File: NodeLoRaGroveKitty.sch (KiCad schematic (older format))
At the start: 37 parts, among them P1 PICKIT PROGRAMMER, P2 Battery, P3 A0, P4 D9, P5 USB-Serial, P6 I2C, SW1 SW_PUSH, SW2 SW_PUSH, U1 AP2112, U2 MCP73831T-2ATI/OT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

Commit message: Fix ADC pin
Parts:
- MODULE1: footprint Library:RN2483 -> TIH:RN2483
- SW1: value SW_PUSH -> SW_BOOT; footprint TIH:SW_SPST_KMR2 -> TIH:SW_B3U-1000P
- SW2: value SW_PUSH -> SW_RESET; footprint TIH:SW_SPST_KMR2 -> TIH:SW_B3U-1000P
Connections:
- net A0: no longer P3.4 (P4)
- net ADC: now also P3.4 (P4)
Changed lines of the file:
@@
 F 0 "MODULE1" H 1650 3550 50  0000 L CNN
 F 1 "RN2903" H 1650 750 50  0000 L CNN
-F 2 "Library:RN2483" H 2250 2150 50  0001 L CNN
+F 2 "TIH:RN2483" H 2250 2150 50  0001 L CNN
 F 3 "None" H 2250 2150 50  0001 L CNN
 F 4 "Sub-GHz Dual Band Long Range Transceiver LoRa Module" H 2250 2150 50  0001 L CNN "Description"
@@
 P 4850 1400
 F 0 "SW2" H 5000 1510 50  0000 C CNN
-F 1 "SW_PUSH" H 4850 1320 50  0000 C CNN
-F 2 "TIH:SW_SPST_KMR2" H 4850 1400 50  0001 C CNN
+F 1 "SW_RESET" H 4850 1320 50  0000 C CNN
+F 2 "TIH:SW_B3U-1000P" H 4850 1400 50  0001 C CNN
 F 3 "" H 4850 1400 50  0000 C CNN
 	1    4850 1400
@@
 $EndComp
 Text Label 9300 5400 0    60   ~ 0
-A0
+ADC
 $Comp
 L GND #PWR017
@@
 P 4830 1965
 F 0 "SW1" H 4980 2075 50  0000 C CNN
-F 1 "SW_PUSH" H 4830 1885 50  0000 C CNN
-F 2 "TIH:SW_SPST_KMR2" H 4830 1965 50  0001 C CNN
+F 1 "SW_BOOT" H 4830 1885 50  0000 C CNN
+F 2 "TIH:SW_B3U-1000P" H 4830 1965 50  0001 C CNN
 F 3 "" H 4830 1965 50  0000 C CNN
 	1    4830 1965

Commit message: Update Grove to 5v
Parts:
- D5: footprint Diodes_SMD:SMA_Handsoldering -> Diodes_SMD:SMB_Handsoldering
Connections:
- net +3V3: no longer P3.2 (P2), P4.2 (P2), P6.2 (P2)
- net A0: now also P3.4 (P4)
- net ADC: no longer P3.4 (P4)
- net VCC: now also P3.2 (P2), P4.2 (P2), P6.2 (P2)
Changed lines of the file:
@@
 $EndComp
 Text Label 9300 5400 0    60   ~ 0
-ADC
+A0
 $Comp
 L GND #PWR017
@@
 $EndComp
 $Comp
-L +3.3V #PWR030
-U 1 1 580964B9
-P 9050 4950
-F 0 "#PWR030" H 9050 4800 50  0001 C CNN
-F 1 "+3.3V" H 9050 5090 50  0000 C CNN
-F 2 "" H 9050 4950 50  0000 C CNN
-F 3 "" H 9050 4950 50  0000 C CNN
-	1    9050 4950
-	1    0    0    -1
-$EndComp
-$Comp
-L +3.3V #PWR031
-U 1 1 58096530
-P 9050 5950
-F 0 "#PWR031" H 9050 5800 50  0001 C CNN
-F 1 "+3.3V" H 9050 6090 50  0000 C CNN
-F 2 "" H 9050 5950 50  0000 C CNN
-F 3 "" H 9050 5950 50  0000 C CNN
-	1    9050 5950
-	1    0    0    -1
-$EndComp
-$Comp
-L +3.3V #PWR032
-U 1 1 580965A7
-P 10250 4950
-F 0 "#PWR032" H 10250 4800 50  0001 C CNN
-F 1 "+3.3V" H 10250 5090 50  0000 C CNN
-F 2 "" H 10250 4950 50  0000 C CNN
-F 3 "" H 10250 4950 50  0000 C CNN
-	1    10250 4950
-	1    0    0    -1
-$EndComp
-$Comp
 L R R8
 U 1 1 58097BD5
@@
 $EndComp
 $Comp
-L GND #PWR033
+L GND #PWR030
 U 1 1 58098088
 P 4560 3870
-F 0 "#PWR033" H 4560 3620 50  0001 C CNN
+F 0 "#PWR030" H 4560 3620 50  0001 C CNN
 F 1 "GND" H 4560 3720 50  0000 C CNN
 F 2 "" H 4560 3870 50  0000 C CNN
@@
 TX
 $Comp
-L GND #PWR034
+L GND #PWR031
 U 1 1 5809B44C
 P 9805 3850
-F 0 "#PWR034" H 9805 3600 50  0001 C CNN
+F 0 "#PWR031" H 9805 3600 50  0001 C CNN
 F 1 "GND" H 9805 3700 50  0000 C CNN
 F 2 "" H 9805 3850 50  0000 C CNN
@@
 $EndComp
 $Comp
-L VCC #PWR035
+L VCC #PWR032
 U 1 1 5809B516
 P 10840 3935
-F 0 "#PWR035" H 10840 3785 50  0001 C CNN
+F 0 "#PWR032" H 10840 3785 50  0001 C CNN
 F 1 "VCC" H 10840 4085 50  0000 C CNN
 F 2 "" H 10840 3935 50  0000 C CNN
@@
 $EndComp
 $Comp
-L PWR_FLAG #FLG036
+L PWR_FLAG #FLG033
 U 1 1 5809BB20
 P 10550 3955
-F 0 "#FLG036" H 10550 4050 50  0001 C CNN
+F 0 "#FLG033" H 10550 4050 50  0001 C CNN
 F 1 "PWR_FLAG" H 10550 4135 50  0000 C CNN
 F 2 "" H 10550 3955 50  0000 C CNN
@@
 $EndComp
 $Comp
-L GND #PWR037
+L GND #PWR034
 U 1 1 5809F5BD
 P 4380 2115
-F 0 "#PWR037" H 4380 1865 50  0001 C CNN
+F 0 "#PWR034" H 4380 1865 50  0001 C CNN
 F 1 "GND" H 4380 1965 50  0000 C CNN
 F 2 "" H 4380 2115 50  0000 C CNN
@@
 F 0 "D5" H 5695 2770 50  0000 C CNN
 F 1 "1N4001" H 5695 2570 50  0000 C CNN
-F 2 "Diodes_SMD:SMA_Handsoldering" H 5695 2670 50  0001 C CNN
+F 2 "Diodes_SMD:SMB_Handsoldering" H 5695 2670 50  0001 C CNN
 F 3 "" H 5695 2670 50  0000 C CNN
 	1    5695 2670
@@
 RX
 NoConn ~ 9925 1685
+$Comp
+L VCC #PWR035
+U 1 1 5850803D
+P 9050 4950
+F 0 "#PWR035" H 9050 4800 50  0001 C CNN
+F 1 "VCC" H 9050 5100 50  0000 C CNN
+F 2 "" H 9050 4950 50  0000 C CNN
+F 3 "" H 9050 4950 50  0000 C CNN
+	1    9050 4950
+	1    0    0    -1
+$EndComp
+$Comp
+L VCC #PWR036
+U 1 1 5850831A
+P 10250 4950
+F 0 "#PWR036" H 10250 4800 50  0001 C CNN
+F 1 "VCC" H 10250 5100 50  0000 C CNN
+F 2 "" H 10250 4950 50  0000 C CNN
+F 3 "" H 10250 4950 50  0000 C CNN
+	1    10250 4950
+	1    0    0    -1
+$EndComp
+$Comp
+L VCC #PWR037
+U 1 1 5850839D
+P 9050 5950
+F 0 "#PWR037" H 9050 5800 50  0001 C CNN
+F 1 "VCC" H 9050 6100 50  0000 C CNN
+F 2 "" H 9050 5950 50  0000 C CNN
+F 3 "" H 9050 5950 50  0000 C CNN
+	1    9050 5950
+	1    0    0    -1
+$EndComp
 $EndSCHEMATC

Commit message: Correct to 3.3v, and R10
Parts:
- added R14: 100K, symbol R
- R10: value 1K2 -> 100K
- R8: value 330R -> 100K
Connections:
- net +3V3: now also P3.2 (P2), P4.2 (P2), P6.2 (P2)
- net A0: now also R14.1; no longer R10.1
- net VCC: no longer P3.2 (P2), P4.2 (P2), P6.2 (P2)
- new net: R10.1, R14.2
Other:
- note added: "Voltage Divider of 3.3v to 1.1v"
- note removed: "Voltage Divider of 5v to 1v"
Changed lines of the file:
@@
 P 4900 3870
 F 0 "R8" V 4980 3870 50  0000 C CNN
-F 1 "330R" V 4900 3870 50  0000 C CNN
+F 1 "100K" V 4900 3870 50  0000 C CNN
 F 2 "Resistors_SMD:R_0805_HandSoldering" V 4830 3870 50  0001 C CNN
 F 3 "" H 4900 3870 50  0000 C CNN
@@
 P 5320 3870
 F 0 "R10" V 5400 3870 50  0000 C CNN
-F 1 "1K2" V 5320 3870 50  0000 C CNN
+F 1 "100K" V 5320 3870 50  0000 C CNN
 F 2 "Resistors_SMD:R_0805_HandSoldering" V 5250 3870 50  0001 C CNN
 F 3 "" H 5320 3870 50  0000 C CNN
@@
 	1    0    0    -1
 $EndComp
-Text Label 5730 3870 0    60   ~ 0
+Text Label 6205 3870 0    60   ~ 0
 A0
 Text Label 5110 3660 0    60   ~ 0
 ADC
 Text Notes 4510 4200 0    60   ~ 0
-Voltage Divider of 5v to 1v
+Voltage Divider of 3.3v to 1.1v
 NoConn ~ 7590 1485
 $Comp
@@
 	4750 3870 4560 3870
 Wire Wire Line
-	5170 3870 5050 3870
+	5050 3870 5170 3870
 Wire Wire Line
 	4840 3195 4840 3295
@@
 	1500 850  1500 800
 Wire Wire Line
-	1400 850  1400 700
-Wire Wire Line
-	1350 850  1400 850
+	1400 700  1400 850
+Wire Wire Line
+	1400 850  1350 850
 Connection ~ 600  850
 Wire Wire Line
@@
 	9550 5100 9300 5100
 Wire Wire Line
-	3650 2450 3650 2350
+	3650 2350 3650 2450
 Connection ~ 3650 2750
 Wire Wire Line
 	3650 2650 3650 2750
 Wire Wire Line
-	3700 2750 3550 2750
+	3550 2750 3700 2750
 Wire Wire Line
 	3150 2850 3700 2850
@@
 Connection ~ 6350 6000
 Wire Wire Line
-	6350 5800 6350 6000
+	6350 6000 6350 5800
 Wire Wire Line
 	5650 6000 6500 6000
@@
 	3800 6200 3900 6200
 Wire Wire Line
-	4250 6200 4100 6200
+	4100 6200 4250 6200
 Connection ~ 6050 6500
 Wire Wire Line
@@
 Connection ~ 1000 6100
 Wire Wire Line
-	1000 6150 1000 6100
+	1000 6100 1000 6150
 Connection ~ 800  6100
 Wire Wire Line
-	800  6150 800  6100
+	800  6100 800  6150
 Connection ~ 1250 6100
 Wire Wire Line
-	1250 6300 1250 6100
+	1250 6100 1250 6300
 Wire Wire Line
 	1350 6300 1250 6300
@@
 NoConn ~ 9925 1685
 $Comp
-L VCC #PWR035
-U 1 1 5850803D
+L R R14
+U 1 1 585145DF
+P 5880 3870
+F 0 "R14" V 5960 3870 50  0000 C CNN
+F 1 "100K" V 5880 3870 50  0000 C CNN
+F 2 "" V 5810 3870 50  0000 C CNN
+F 3 "" H 5880 3870 50  0000 C CNN
+	1    5880 3870
+	0    1    1    0
+$EndComp
+Wire Wire Line
+	6030 3870 6205 3870
+$Comp
+L +3.3V #PWR035
+U 1 1 58514B84
 P 9050 4950
 F 0 "#PWR035" H 9050 4800 50  0001 C CNN
-F 1 "VCC" H 9050 5100 50  0000 C CNN
+F 1 "+3.3V" H 9050 5090 50  0000 C CNN
 F 2 "" H 9050 4950 50  0000 C CNN
 F 3 "" H 9050 4950 50  0000 C CNN
@@
 $EndComp
 $Comp
-L VCC #PWR036
-U 1 1 5850831A
+L +3.3V #PWR036
+U 1 1 58514F58
 P 10250 4950
 F 0 "#PWR036" H 10250 4800 50  0001 C CNN
-F 1 "VCC" H 10250 5100 50  0000 C CNN
+F 1 "+3.3V" H 10250 5090 50  0000 C CNN
 F 2 "" H 10250 4950 50  0000 C CNN
 F 3 "" H 10250 4950 50  0000 C CNN
@@
 $EndComp
 $Comp
-L VCC #PWR037
-U 1 1 5850839D
+L +3.3V #PWR037
+U 1 1 585150D6
 P 9050 5950
 F 0 "#PWR037" H 9050 5800 50  0001 C CNN
-F 1 "VCC" H 9050 6100 50  0000 C CNN
+F 1 "+3.3V" H 9050 6090 50  0000 C CNN
 F 2 "" H 9050 5950 50  0000 C CNN
 F 3 "" H 9050 5950 50  0000 C CNN

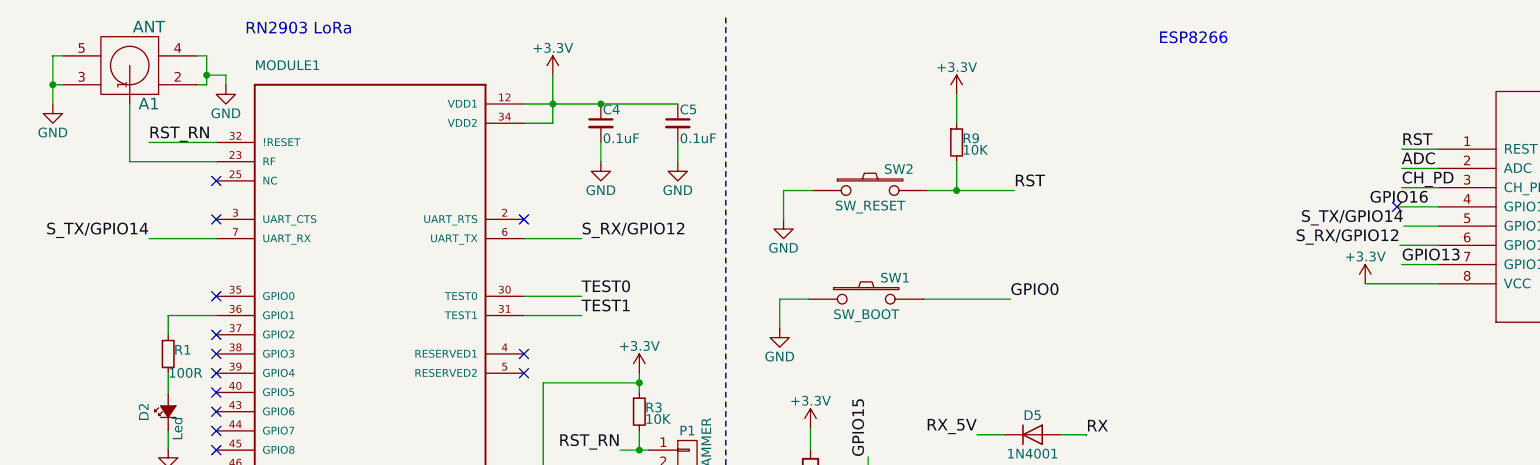
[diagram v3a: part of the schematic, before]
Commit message: Fix pines S_TX and S_RX
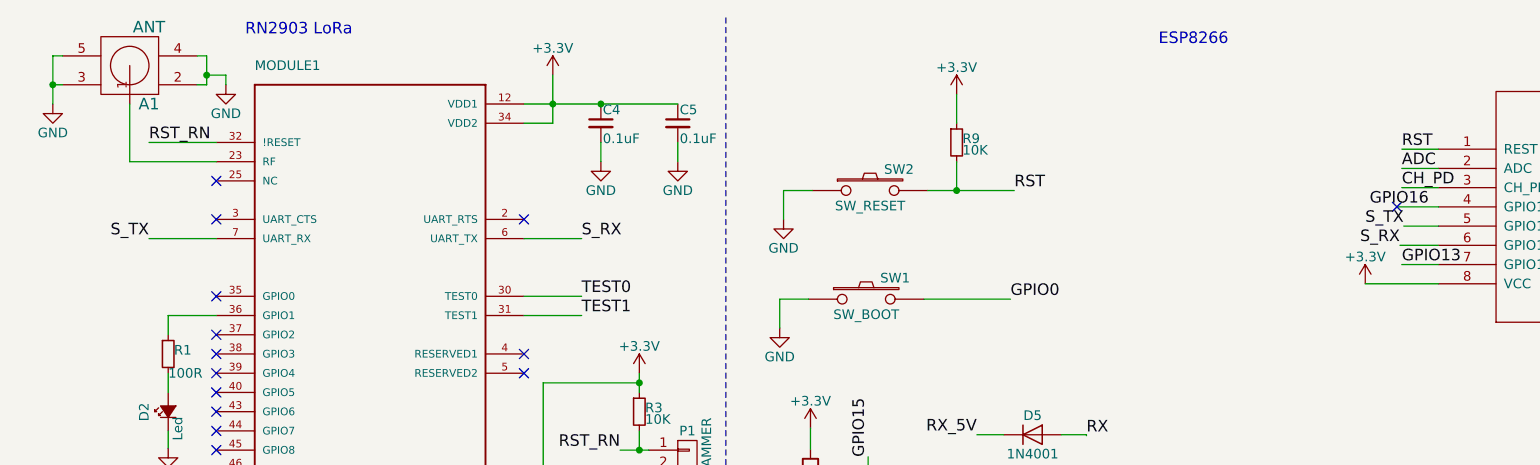
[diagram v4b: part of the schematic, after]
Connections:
- net S_RX/GPIO12 renamed S_RX
- net S_TX/GPIO14 renamed S_TX
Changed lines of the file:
@@
 TEST1
 Text Label 3350 1650 0    60   ~ 0
-S_RX/GPIO12
+S_RX
 Text Label 1100 1650 2    60   ~ 0
-S_TX/GPIO14
+S_TX
 Text Label 1100 1150 0    60   ~ 0
 RST_RN
@@
 GPIO16
 Text Label 7625 1585 2    60   ~ 0
-S_TX/GPIO14
+S_TX
 Text Label 7605 1685 2    60   ~ 0
-S_RX/GPIO12
+S_RX
 Text Label 7615 1785 0    60   ~ 0
 GPIO13

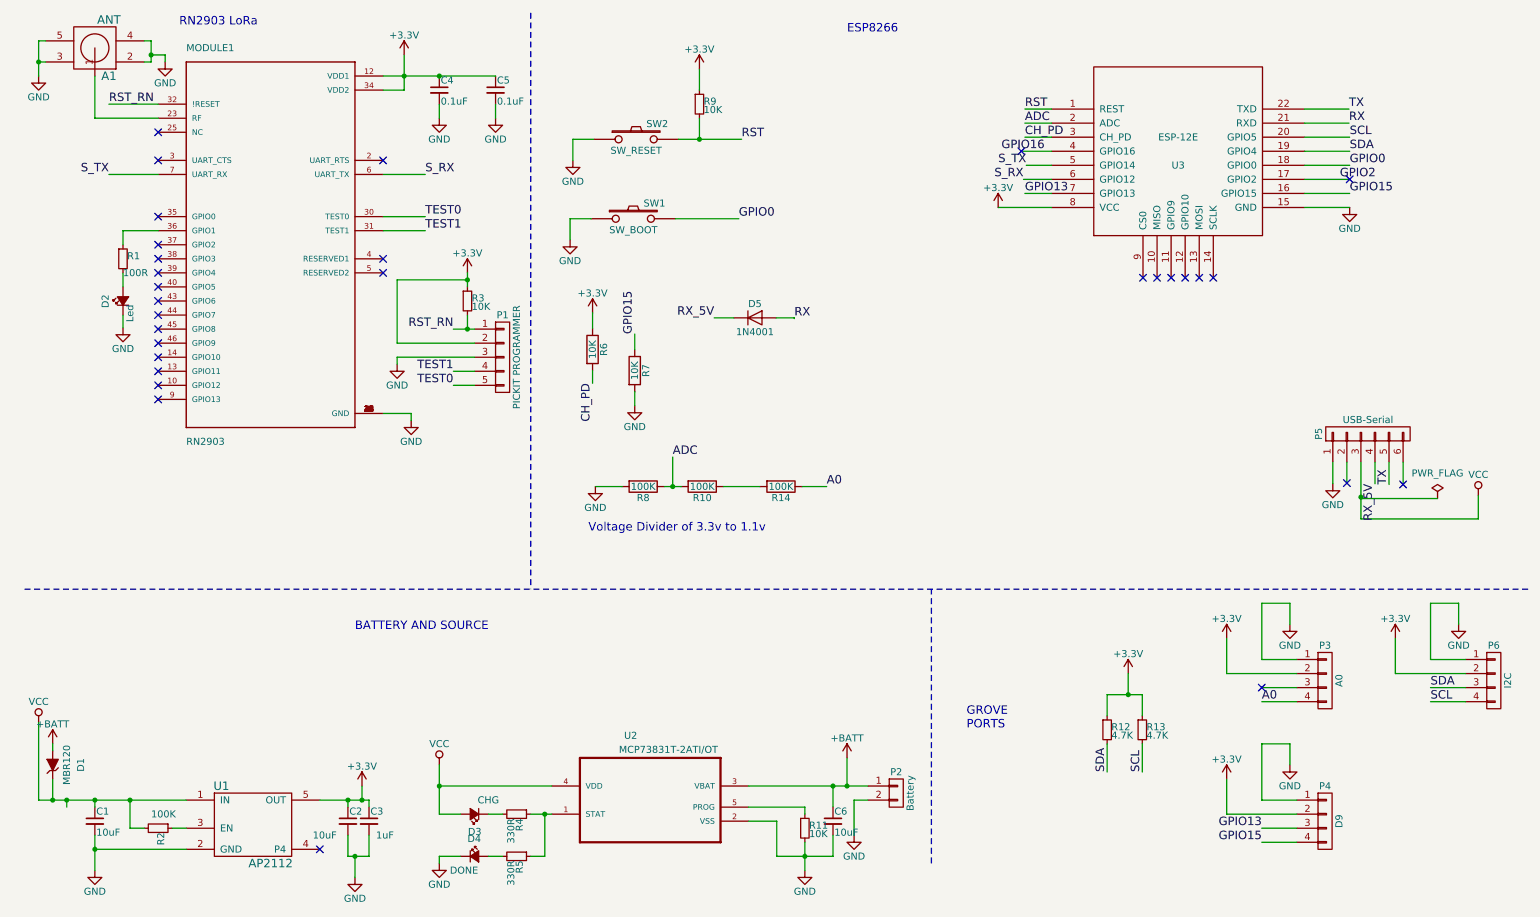
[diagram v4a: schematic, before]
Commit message: Change GPIO2
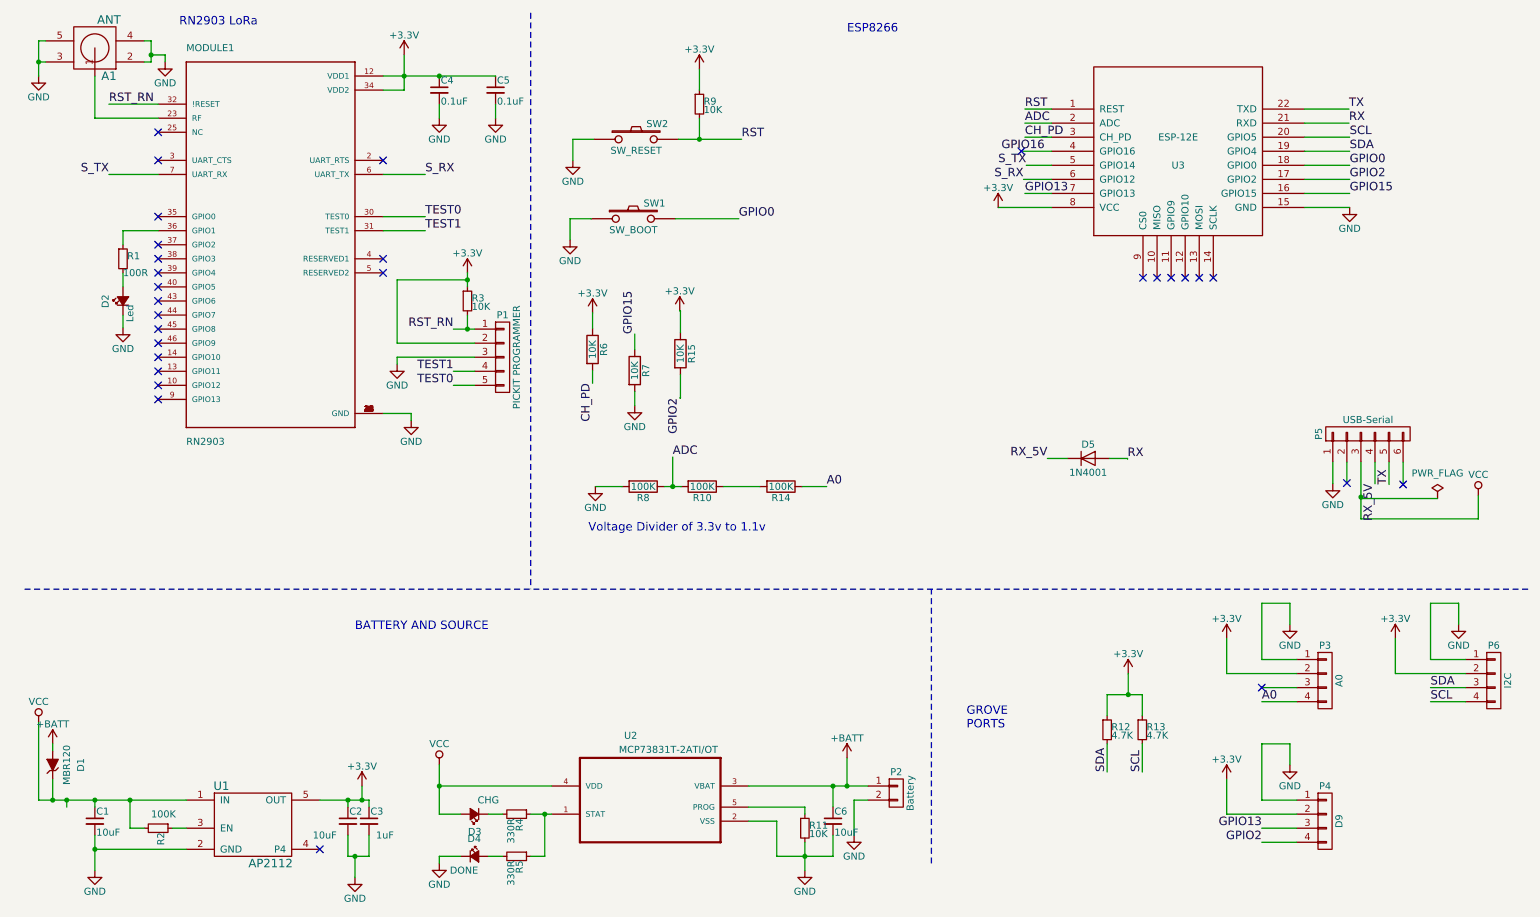
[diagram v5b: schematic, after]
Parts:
- added R15: 10K, Resistors_SMD:R_0805_HandSoldering, symbol R
- R14: footprint (none) -> Resistors_SMD:R_0805_HandSoldering
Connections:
- net +3V3: now also R15.1
- net GPIO15: no longer P4.4 (P4)
- net GPIO2: now also P4.4 (P4), R15.2
- no-connect marks 30 -> 29
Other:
- moved on the sheet: D5
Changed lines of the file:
@@
 Sheet 1 1
 Title "LoRaCat: Kitty"
-Date "2016-10-20"
-Rev "0.2"
+Date "2016-12-16"
+Rev "0.3"
 Comp "Electronic Cats"
 Comment1 "Andres Sabas"
@@
 $EndComp
 Text Label 9300 6400 2    60   ~ 0
-GPIO15
+GPIO2
 Text Label 9300 6300 2    60   ~ 0
 GPIO13
@@
 Text Label 9925 1585 0    60   ~ 0
 GPIO0
-Text Label 9855 1685 0    60   ~ 0
+Text Label 9925 1685 0    60   ~ 0
 GPIO2
 Text Label 9925 1785 0    60   ~ 0
@@
 L D D5
 U 1 1 580A2F07
-P 5695 2670
-F 0 "D5" H 5695 2770 50  0000 C CNN
-F 1 "1N4001" H 5695 2570 50  0000 C CNN
-F 2 "Diodes_SMD:SMB_Handsoldering" H 5695 2670 50  0001 C CNN
-F 3 "" H 5695 2670 50  0000 C CNN
-	1    5695 2670
+P 8065 3670
+F 0 "D5" H 8065 3770 50  0000 C CNN
+F 1 "1N4001" H 8065 3570 50  0000 C CNN
+F 2 "Diodes_SMD:SMB_Handsoldering" H 8065 3670 50  0001 C CNN
+F 3 "" H 8065 3670 50  0000 C CNN
+	1    8065 3670
 	1    0    0    -1
 $EndComp
@@
 	1250 6100 1250 6300
 Wire Wire Line
-	1350 6300 1250 6300
+	1250 6300 1350 6300
 Wire Wire Line
 	1550 6300 1650 6300
@@
 	5130 1965 5580 1965
 Wire Wire Line
-	5845 2670 5975 2670
-Wire Wire Line
-	5975 2670 5975 2675
-Wire Wire Line
-	5545 2670 5405 2670
-Text Label 5405 2670 2    60   ~ 0
+	8215 3670 8345 3670
+Wire Wire Line
+	8345 3670 8345 3675
+Wire Wire Line
+	7915 3670 7775 3670
+Text Label 7775 3670 2    60   ~ 0
 RX_5V
-Text Label 5975 2675 0    60   ~ 0
+Text Label 8345 3675 0    60   ~ 0
 RX
-NoConn ~ 9925 1685
 $Comp
 L R R14
@@
 F 0 "R14" V 5960 3870 50  0000 C CNN
 F 1 "100K" V 5880 3870 50  0000 C CNN
-F 2 "" V 5810 3870 50  0000 C CNN
+F 2 "Resistors_SMD:R_0805_HandSoldering" V 5810 3870 50  0001 C CNN
 F 3 "" H 5880 3870 50  0000 C CNN
 	1    5880 3870
@@
 	1    0    0    -1
 $EndComp
+$Comp
+L R R15
+U 1 1 58543F5A
+P 5165 2925
+F 0 "R15" V 5245 2925 50  0000 C CNN
+F 1 "10K" V 5165 2925 50  0000 C CNN
+F 2 "Resistors_SMD:R_0805_HandSoldering" V 5095 2925 50  0001 C CNN
+F 3 "" H 5165 2925 50  0000 C CNN
+	1    5165 2925
+	1    0    0    -1
+$EndComp
+Wire Wire Line
+	5165 2775 5165 2620
+Wire Wire Line
+	5165 2620 5160 2620
+Wire Wire Line
+	5165 3075 5165 3240
+Wire Wire Line
+	5165 3240 5160 3240
+Text Label 5160 3240 3    60   ~ 0
+GPIO2
+$Comp
+L +3.3V #PWR038
+U 1 1 5854483F
+P 5160 2620
+F 0 "#PWR038" H 5160 2470 50  0001 C CNN
+F 1 "+3.3V" H 5160 2760 50  0000 C CNN
+F 2 "" H 5160 2620 50  0000 C CNN
+F 3 "" H 5160 2620 50  0000 C CNN
+	1    5160 2620
+	1    0    0    -1
+$EndComp

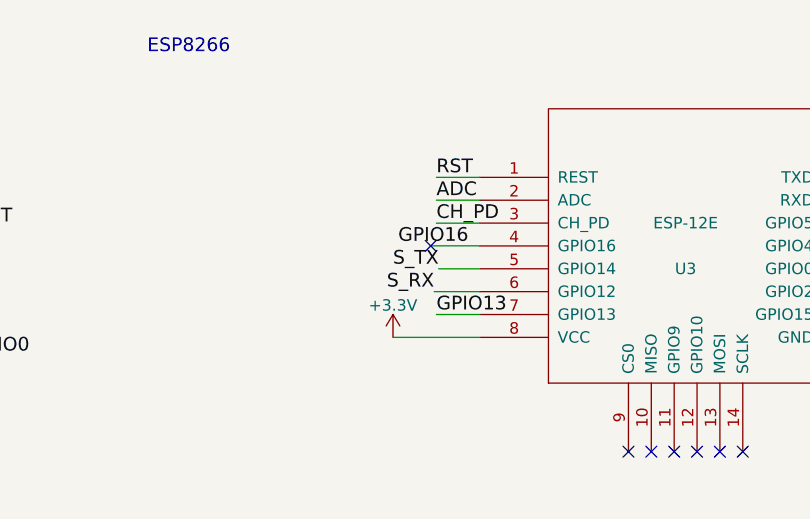
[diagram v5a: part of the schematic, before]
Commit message: Add pin reset for RN
GPIO16
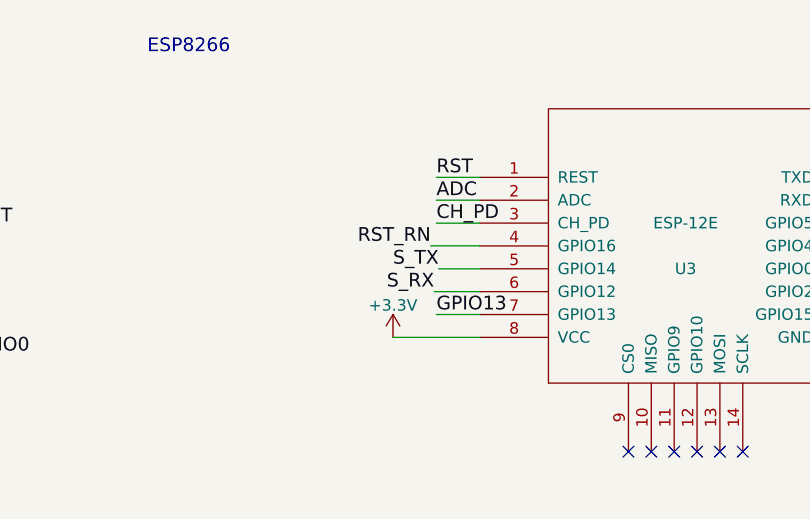
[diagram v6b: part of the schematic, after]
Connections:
- net GPIO16 is gone; now on net RST_RN: U3.4 (GPIO16)
- no-connect marks 29 -> 28
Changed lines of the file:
@@
 Sheet 1 1
 Title "LoRaCat: Kitty"
-Date "2016-12-16"
-Rev "0.3"
+Date "2017-01-2"
+Rev "0.4"
 Comp "Electronic Cats"
 Comment1 "Andres Sabas"
@@
 Text Label 7615 1385 0    60   ~ 0
 CH_PD
-Text Label 7755 1485 2    60   ~ 0
-GPIO16
+Text Label 7590 1485 2    60   ~ 0
+RST_RN
 Text Label 7625 1585 2    60   ~ 0
 S_TX
@@
 Text Notes 4510 4200 0    60   ~ 0
 Voltage Divider of 3.3v to 1.1v
-NoConn ~ 7590 1485
 $Comp
 L CONN_01X06 P5
